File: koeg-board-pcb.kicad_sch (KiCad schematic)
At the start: 5 parts

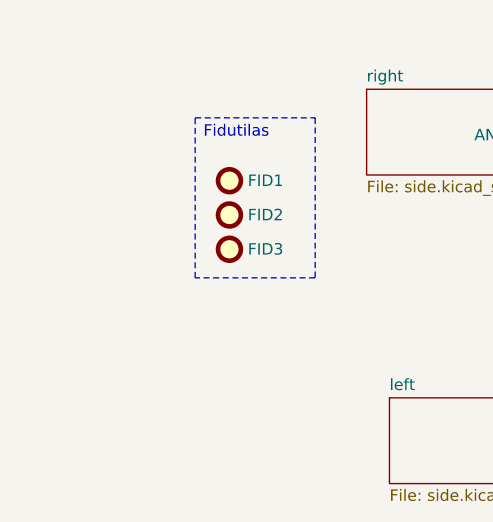
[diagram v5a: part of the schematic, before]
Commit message: added mousebites properly this time
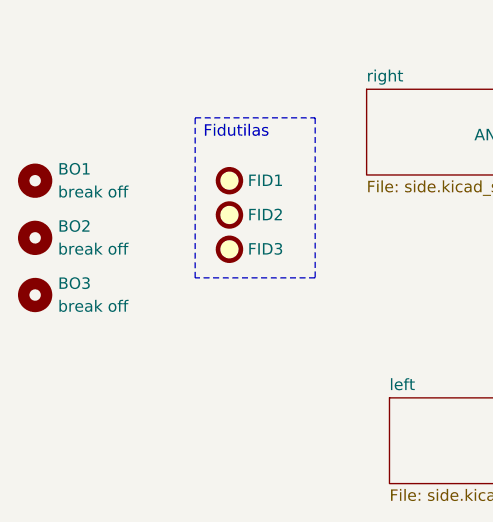
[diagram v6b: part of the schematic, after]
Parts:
- added BO1, BO2, BO3: break off, panelization:mouse-bite-2mm-slot, symbol Mechanical:MountingHole
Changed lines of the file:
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@@
 (kicad_sch
-	(version 20231120)
+	(version 20241004)
 	(generator "eeschema")
-	(generator_version "8.0")
+	(generator_version "8.99")
 	(paper "A4")
-	(wire
-		(pts
-			(xy 146.685 139.7) (xy 158.75 139.7)
-		)
-		(stroke
-			(width 0)
-			(type default)
-		)
-	)
-	(wire
-		(pts
-			(xy 158.75 107.95) (xy 158.75 105.41)
-		)
-		(stroke
-			(width 0)
-			(type default)
-		)
-	)
-	(wire
-		(pts
-			(xy 144.145 105.41) (xy 153.67 105.41)
-		)
-		(stroke
-			(width 0)
-			(type default)
-		)
-	)
-	(wire
-		(pts
-			(xy 163.83 142.24) (xy 163.83 139.7)
-		)
-		(stroke
-			(width 0)
-			(type default)
-		)
-	)
 	(rectangle
 		(start 107.95 103.505)
@@
 		)
 	)
+	(wire
+		(pts
+			(xy 146.685 139.7) (xy 158.75 139.7)
+		)
+		(stroke
+			(width 0)
+			(type default)
+		)
+	)
+	(wire
+		(pts
+			(xy 158.75 107.95) (xy 158.75 105.41)
+		)
+		(stroke
+			(width 0)
+			(type default)
+		)
+	)
+	(wire
+		(pts
+			(xy 144.145 105.41) (xy 153.67 105.41)
+		)
+		(stroke
+			(width 0)
+			(type default)
+		)
+	)
+	(wire
+		(pts
+			(xy 163.83 142.24) (xy 163.83 139.7)
+		)
+		(stroke
+			(width 0)
+			(type default)
+		)
+	)
 	(symbol
 		(lib_id "Device:Antenna_Chip")
@@
 	)
 	(symbol
+		(lib_id "Mechanical:MountingHole")
+		(at 90.17 123.19 0)
+		(unit 1)
+		(exclude_from_sim yes)
+		(in_bom no)
+		(on_board yes)
+		(dnp no)
+		(fields_autoplaced yes)
+		(property "Reference" "BO3"
+			(at 92.71 121.9199 0)
+			(effects
+				(font
+					(size 1.27 1.27)
+				)
+				(justify left)
+			)
+		)
+		(property "Value" "break off"
+			(at 92.71 124.4599 0)
+			(effects
+				(font
+					(size 1.27 1.27)
+				)
+				(justify left)
+			)
+		)
+		(property "Footprint" "panelization:mouse-bite-2mm-slot"
+			(at 90.17 123.19 0)
+			(effects
+				(font
+					(size 1.27 1.27)
+				)
+				(hide yes)
+			)
+		)
+		(property "Datasheet" "~"
+			(at 90.17 123.19 0)
+			(effects
+				(font
+					(size 1.27 1.27)
+				)
+				(hide yes)
+			)
+		)
+		(property "Description" "Mounting Hole without connection"
+			(at 90.17 123.19 0)
+			(effects
+				(font
+					(size 1.27 1.27)
+				)
+				(hide yes)
+			)
+		)
+		(instances
+			(project "koeg-board-pcb"
+				(path "/2b736a6b-c6e2-42fa-94c9-e384d663659b"
+					(reference "BO3")
+					(unit 1)
+				)
+			)
+		)
+	)
+	(symbol
 		(lib_id "power:GND")
 		(at 158.75 107.95 0)
@@
 	)
 	(symbol
+		(lib_id "Mechanical:MountingHole")
+		(at 90.17 116.84 0)
+		(unit 1)
+		(exclude_from_sim yes)
+		(in_bom no)
+		(on_board yes)
+		(dnp no)
+		(fields_autoplaced yes)
+		(property "Reference" "BO2"
+			(at 92.71 115.5699 0)
+			(effects
+				(font
+					(size 1.27 1.27)
+				)
+				(justify left)
+			)
+		)
+		(property "Value" "break off"
+			(at 92.71 118.1099 0)
+			(effects
+				(font
+					(size 1.27 1.27)
+				)
+				(justify left)
+			)
+		)
+		(property "Footprint" "panelization:mouse-bite-2mm-slot"
+			(at 90.17 116.84 0)
+			(effects
+				(font
+					(size 1.27 1.27)
+				)
+				(hide yes)
+			)
+		)
+		(property "Datasheet" "~"
+			(at 90.17 116.84 0)
+			(effects
+				(font
+					(size 1.27 1.27)
+				)
+				(hide yes)
+			)
+		)
+		(property "Description" "Mounting Hole without connection"
+			(at 90.17 116.84 0)
+			(effects
+				(font
+					(size 1.27 1.27)
+				)
+				(hide yes)
+			)
+		)
+		(instances
+			(project "koeg-board-pcb"
+				(path "/2b736a6b-c6e2-42fa-94c9-e384d663659b"
+					(reference "BO2")
+					(unit 1)
+				)
+			)
+		)
+	)
+	(symbol
 		(lib_id "power:GND")
 		(at 163.83 142.24 0)
@@
 	)
 	(symbol
+		(lib_id "Mechanical:MountingHole")
+		(at 90.17 110.49 0)
+		(unit 1)
+		(exclude_from_sim yes)
+		(in_bom no)
+		(on_board yes)
+		(dnp no)
+		(fields_autoplaced yes)
+		(property "Reference" "BO1"
+			(at 92.71 109.2199 0)
+			(effects
+				(font
+					(size 1.27 1.27)
+				)
+				(justify left)
+			)
+		)
+		(property "Value" "break off"
+			(at 92.71 111.7599 0)
+			(effects
+				(font
+					(size 1.27 1.27)
+				)
+				(justify left)
+			)
+		)
+		(property "Footprint" "panelization:mouse-bite-2mm-slot"
+			(at 90.17 110.49 0)
+			(effects
+				(font
+					(size 1.27 1.27)
+				)
+				(hide yes)
+			)
+		)
+		(property "Datasheet" "~"
+			(at 90.17 110.49 0)
+			(effects
+				(font
+					(size 1.27 1.27)
+				)
+				(hide yes)
+			)
+		)
+		(property "Description" "Mounting Hole without connection"
+			(at 90.17 110.49 0)
+			(effects
+				(font
+					(size 1.27 1.27)
+				)
+				(hide yes)
+			)
+		)
+		(instances
+			(project ""
+				(path "/2b736a6b-c6e2-42fa-94c9-e384d663659b"
+					(reference "BO1")
+					(unit 1)
+				)
+			)
+		)
+	)
+	(symbol
 		(lib_id "Mechanical:Fiducial")
 		(at 111.76 118.11 0)
@@
 		(at 129.54 134.62)
 		(size 17.145 9.525)
+		(exclude_from_sim no)
+		(in_bom yes)
+		(on_board yes)
+		(dnp no)
 		(fields_autoplaced yes)
 		(stroke
@@
 		(at 127 100.33)
 		(size 17.145 9.525)
+		(exclude_from_sim no)
+		(in_bom yes)
+		(on_board yes)
+		(dnp no)
 		(fields_autoplaced yes)
 		(stroke
@@
 		)
 	)
+	(embedded_fonts no)
 )

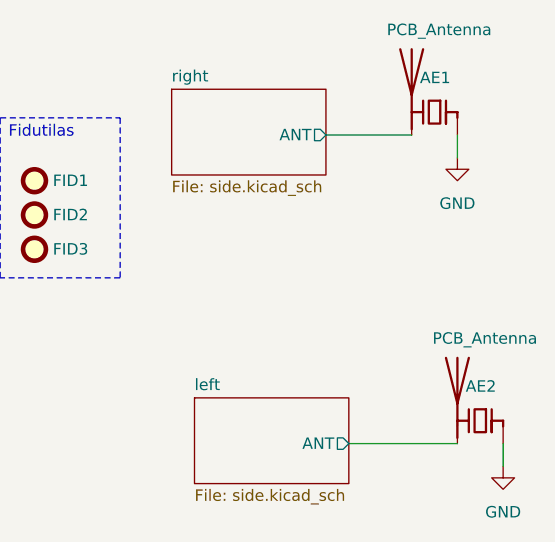
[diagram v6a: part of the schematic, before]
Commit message: switched to chip antenna
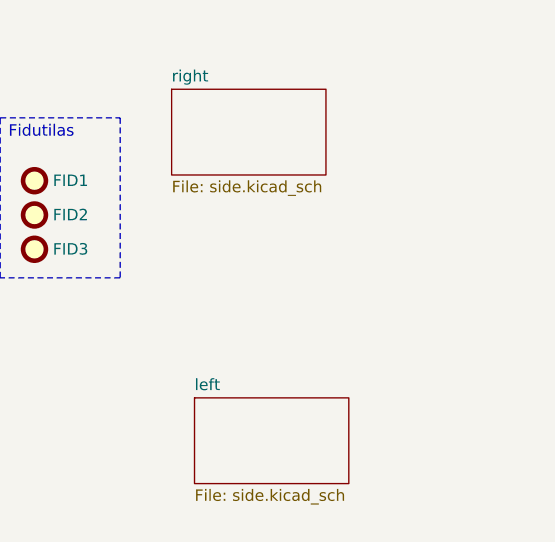
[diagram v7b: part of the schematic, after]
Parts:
- removed AE1: PCB_Antenna, pcb_ant:flipped_pcb_antenna, symbol Device:Antenna_Chip
- removed AE2: PCB_Antenna, pcb_ant:pcb_antenna, symbol Device:Antenna_Chip
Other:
- sheet left ports: added none; removed ANT
- sheet right ports: added none; removed ANT
